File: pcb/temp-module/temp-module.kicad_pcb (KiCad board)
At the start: 2 copper layers, 37 x 27 mm, 14 parts, among them J1 Connector_male, J2 Screw_Terminal_01x02, U1 MCP6002-xSN

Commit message: update pcb
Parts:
- J2: footprint TerminalBlock:TerminalBlock_bornier-2_P5.08mm -> TerminalBlock_Phoenix:TerminalBlock_Phoenix_MKDS-1,5-2-5.08_1x02_P5.08mm_Horizontal
- R1: value 1.3K -> 110K
- R3: value 5.1K -> 1.3K
- R4: value 330R -> 5.1K
- R5: value 5.1K -> 330R
- R6: value 110K -> 5.1K
- moved R3 17.2 mm to (150.9, 101.0)
- moved R6 17.1 mm to (166.5, 101.0)
- moved R1 7.09 mm to (150.9, 94.0)
- moved J2 5.21 mm to (157.4, 111.0), turned to 0 degrees
- moved R4 3.90 mm to (166.5, 94.0)
- moved R5 3.89 mm to (166.5, 97.5)
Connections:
- R1 pad 1: S1 -> /U5_OP-
- R1 pad 2: GND -> SREG
- R3 pad 1: GND -> S1
- R3 pad 2: /R4-5 -> GND
- R4 pad 1: /R4-5 -> +5V
- R5 pad 1: +5V -> /R4-5
- R6 pad 1: /U5_OP- -> GND
- R6 pad 2: SREG -> /R4-5
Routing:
- net SREG: track 65.3 -> 30.1 mm
- net +5V: track 78.5 -> 63.4 mm
- net S1: track 21.4 -> 16.6 mm
- net GND: track 33.6 -> 32.4 mm
- net /U5_OP+: track 22.0 -> 20.8 mm
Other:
- board text added: "Sensor"

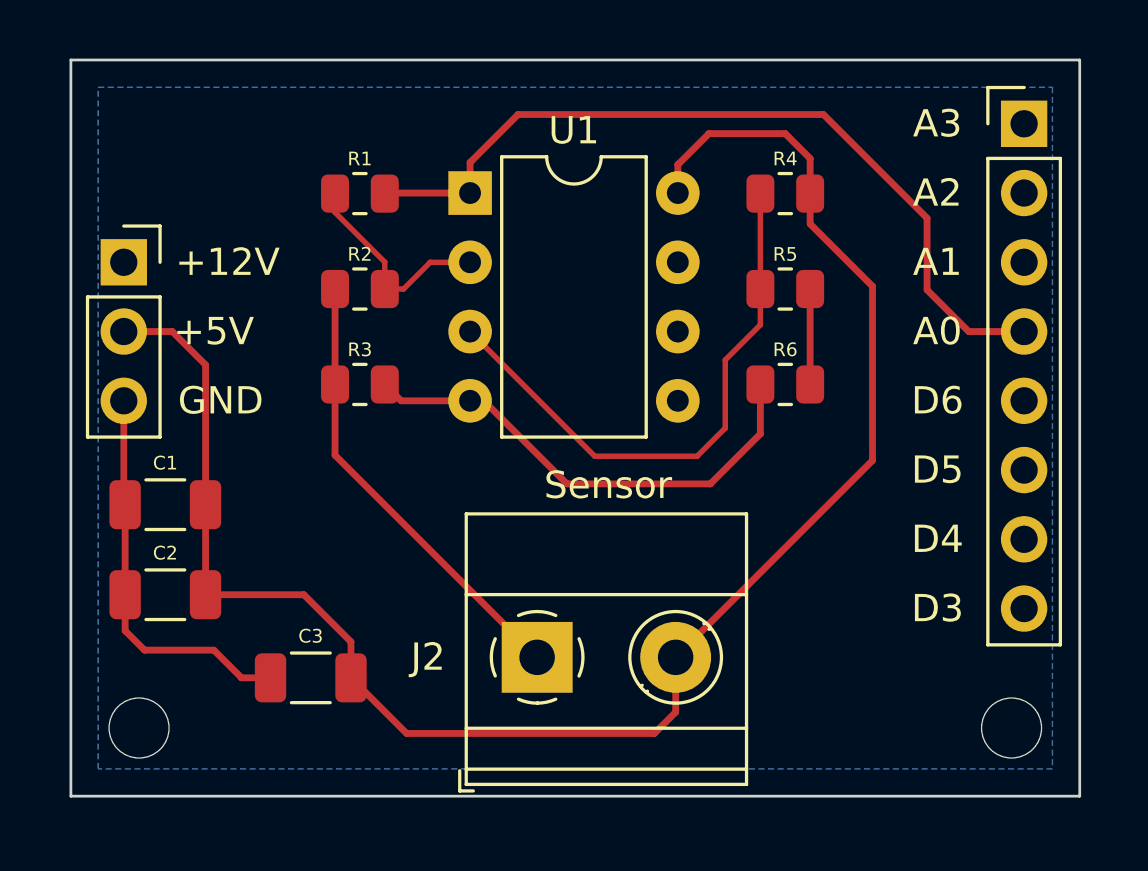
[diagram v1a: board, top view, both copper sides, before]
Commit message: added AVRISP adapter to pcb
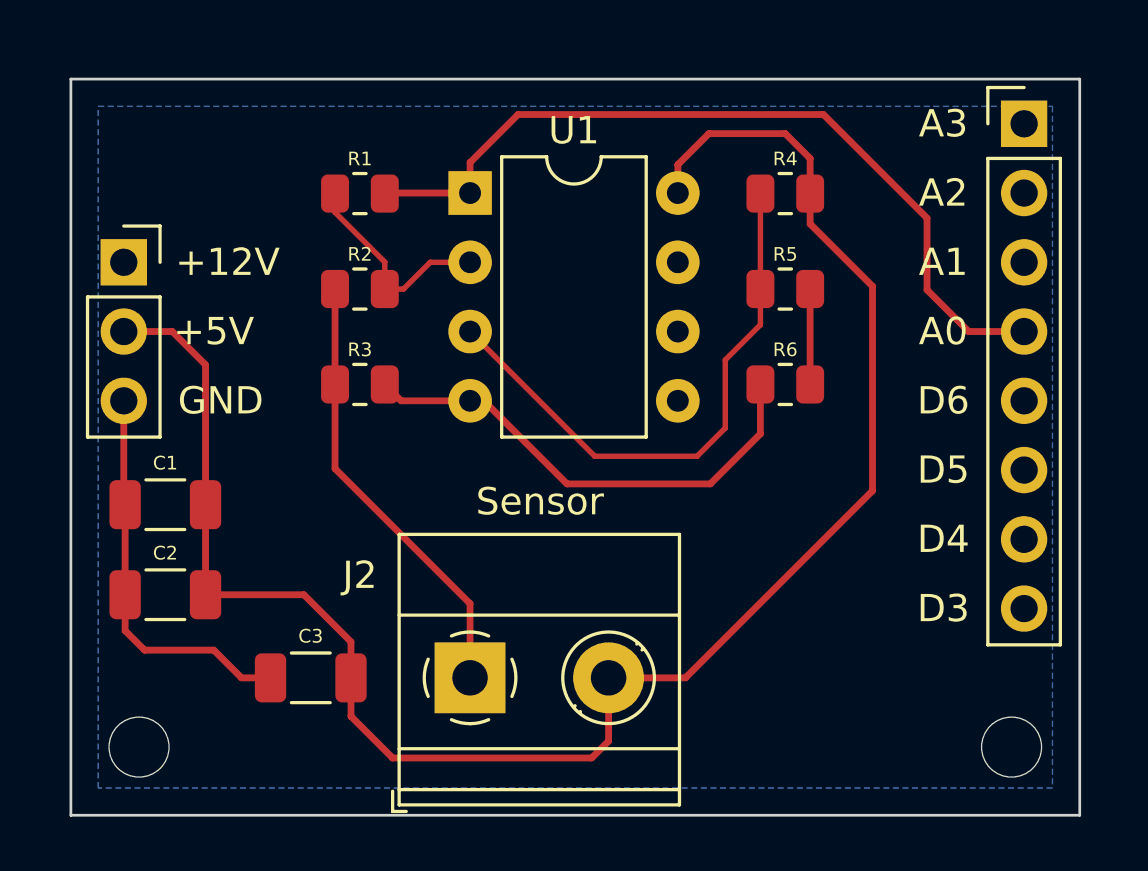
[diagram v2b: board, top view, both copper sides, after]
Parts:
- moved J2 2.57 mm to (154.9, 111.8)
- moved REF** 0.70 mm to (174.8, 114.3)
- moved REF** 0.70 mm to (142.8, 114.3)
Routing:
- net +5V: track 63.4 -> 65.8 mm
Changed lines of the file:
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@@
       (effects (font (size 1 1) (thickness 0.15)))
     )
-    (fp_text user "D4" (at 14.605 7.62 unlocked) (layer "F.SilkS")
-      (effects (font (size 1 1) (thickness 0.15)))
-    )
-    (fp_text user "A1" (at 14.605 -2.54 unlocked) (layer "F.SilkS")
-      (effects (font (size 1 1) (thickness 0.15)))
-    )
-    (fp_text user "A0" (at 14.605 0 unlocked) (layer "F.SilkS")
-      (effects (font (size 1 1) (thickness 0.15)))
-    )
-    (fp_text user "D3" (at 14.605 10.16 unlocked) (layer "F.SilkS")
-      (effects (font (size 1 1) (thickness 0.15)))
-    )
-    (fp_text user "D5" (at 14.605 5.08 unlocked) (layer "F.SilkS")
+    (fp_text user "D4" (at 14.82 7.62 unlocked) (layer "F.SilkS")
+      (effects (font (size 1 1) (thickness 0.15)))
+    )
+    (fp_text user "A1" (at 14.82 -2.54 unlocked) (layer "F.SilkS")
+      (effects (font (size 1 1) (thickness 0.15)))
+    )
+    (fp_text user "A0" (at 14.82 0 unlocked) (layer "F.SilkS")
+      (effects (font (size 1 1) (thickness 0.15)))
+    )
+    (fp_text user "D3" (at 14.82 10.16 unlocked) (layer "F.SilkS")
+      (effects (font (size 1 1) (thickness 0.15)))
+    )
+    (fp_text user "D5" (at 14.82 5.08 unlocked) (layer "F.SilkS")
       (effects (font (size 1 1) (thickness 0.15)))
     )
@@
       (effects (font (size 1 1) (thickness 0.15)))
     )
-    (fp_text user "A3" (at 14.605 -7.62 unlocked) (layer "F.SilkS")
-      (effects (font (size 1 1) (thickness 0.15)))
-    )
-    (fp_text user "A2" (at 14.605 -5.08 unlocked) (layer "F.SilkS")
-      (effects (font (size 1 1) (thickness 0.15)))
-    )
-    (fp_text user "D6" (at 14.605 2.54 unlocked) (layer "F.SilkS")
+    (fp_text user "A3" (at 14.82 -7.62 unlocked) (layer "F.SilkS")
+      (effects (font (size 1 1) (thickness 0.15)))
+    )
+    (fp_text user "A2" (at 14.82 -5.08 unlocked) (layer "F.SilkS")
+      (effects (font (size 1 1) (thickness 0.15)))
+    )
+    (fp_text user "D6" (at 14.82 2.54 unlocked) (layer "F.SilkS")
       (effects (font (size 1 1) (thickness 0.15)))
     )
@@
   )
   (footprint "MountingHole:MountingHole_2.2mm_M2" (layer "F.Cu")
-    (at 174.8 113.6)
+    (at 174.8 114.3)
     (descr "Mounting Hole 2.2mm, no annular, M2")
     (tags "mounting hole 2.2mm no annular m2")
@@
   )
   (footprint "MountingHole:MountingHole_2.2mm_M2" (layer "F.Cu")
-    (at 142.8 113.6)
+    (at 142.8 114.3)
     (descr "Mounting Hole 2.2mm, no annular, M2")
     (tags "mounting hole 2.2mm no annular m2")
@@
   )
   (footprint "TerminalBlock_Phoenix:TerminalBlock_Phoenix_MKDS-1,5-2-5.08_1x02_P5.08mm_Horizontal" (layer "F.Cu")
-    (at 157.4 111.0085)
+    (at 154.94 111.76)
     (descr "Terminal Block Phoenix MKDS-1,5-2-5.08, 2 pins, pitch 5.08mm, size 10.2x9.8mm^2, drill diamater 1.3mm, pad diameter 2.6mm, see http://www.farnell.com/datasheets/100425.pdf, script-generated using https://github.com/pointhi/kicad-footprint-generator/scripts/TerminalBlock_Phoenix")
     (tags "THT Terminal Block Phoenix MKDS-1,5-2-5.08 pitch 5.08mm size 10.2x9.8mm^2 drill 1.3mm pad 2.6mm")
@@
     (property "Sheetname" "")
     (attr through_hole)
-    (fp_text reference "J2" (at -4 -0.0085) (layer "F.SilkS")
+    (fp_text reference "J2" (at -4.04 -3.76) (layer "F.SilkS")
       (effects (font (size 1 1) (thickness 0.15)))
     )
@@
     )
   )
-  (gr_line (start 140.3 89.1) (end 140.3 116.1) (layer "Edge.Cuts") (width 0.1))
-  (gr_line (start 177.3 89.1) (end 140.3 89.1) (layer "Edge.Cuts") (width 0.1))
-  (gr_line (start 140.3 116.1) (end 177.3 116.1) (layer "Edge.Cuts") (width 0.1))
-  (gr_line (start 177.3 116.1) (end 177.3 89.1) (layer "Edge.Cuts") (width 0.1))
+  (gr_line (start 140.3 89.8) (end 140.3 116.8) (layer "Edge.Cuts") (width 0.1))
+  (gr_line (start 177.3 89.8) (end 140.3 89.8) (layer "Edge.Cuts") (width 0.1))
+  (gr_line (start 140.3 116.8) (end 177.3 116.8) (layer "Edge.Cuts") (width 0.1))
+  (gr_line (start 177.3 116.8) (end 177.3 89.8) (layer "Edge.Cuts") (width 0.1))
   (gr_text "GND" (at 145.796 101.6) (layer "F.SilkS")
     (effects (font (size 1 1) (thickness 0.15)))
   )
-  (gr_text "Sensor" (at 160 104.7) (layer "F.SilkS")
+  (gr_text "Sensor" (at 157.5 105.3) (layer "F.SilkS")
     (effects (font (size 1 1) (thickness 0.15)))
   )
-  (segment (start 149.9875 103.596) (end 157.4 111.0085) (width 0.25) (layer "F.Cu") (net 1))
-  (segment (start 149.9875 101) (end 149.9875 103.596) (width 0.25) (layer "F.Cu") (net 1))
+  (segment (start 154.94 109.04) (end 149.9875 104.0875) (width 0.25) (layer "F.Cu") (net 1))
   (segment (start 149.9875 97.5) (end 149.9875 101) (width 0.25) (layer "F.Cu") (net 1))
-  (segment (start 162.48 113.02) (end 162.48 111.0085) (width 0.25) (layer "F.Cu") (net 2))
-  (segment (start 152.613 113.8) (end 161.7 113.8) (width 0.25) (layer "F.Cu") (net 2))
+  (segment (start 149.9875 104.0875) (end 149.9875 101) (width 0.25) (layer "F.Cu") (net 1))
+  (segment (start 154.94 111.76) (end 154.94 109.04) (width 0.25) (layer "F.Cu") (net 1))
+  (segment (start 152.1 114.7) (end 159.4 114.7) (width 0.25) (layer "F.Cu") (net 2))
   (segment (start 145.239 100.281) (end 144.018 99.06) (width 0.25) (layer "F.Cu") (net 2))
   (segment (start 144.018 99.06) (end 142.24 99.06) (width 0.25) (layer "F.Cu") (net 2))
+  (segment (start 150.573 111.76) (end 150.573 113.173) (width 0.25) (layer "F.Cu") (net 2))
   (segment (start 150.573 111.76) (end 150.573 110.441) (width 0.25) (layer "F.Cu") (net 2))
+  (segment (start 159.4 114.7) (end 160.02 114.08) (width 0.25) (layer "F.Cu") (net 2))
   (segment (start 163.7 91.8) (end 162.56 92.94) (width 0.25) (layer "F.Cu") (net 2))
   (segment (start 167.4125 92.7125) (end 166.5 91.8) (width 0.25) (layer "F.Cu") (net 2))
+  (segment (start 169.7 104.9) (end 169.7 97.4) (width 0.25) (layer "F.Cu") (net 2))
   (segment (start 167.4125 94) (end 167.4125 92.7125) (width 0.25) (layer "F.Cu") (net 2))
+  (segment (start 160.02 111.76) (end 162.84 111.76) (width 0.25) (layer "F.Cu") (net 2))
   (segment (start 148.844 108.712) (end 150.573 110.441) (width 0.25) (layer "F.Cu") (net 2))
-  (segment (start 169.7 103.7885) (end 169.7 97.4) (width 0.25) (layer "F.Cu") (net 2))
   (segment (start 145.239 105.41) (end 145.239 108.712) (width 0.25) (layer "F.Cu") (net 2))
   (segment (start 166.5 91.8) (end 163.7 91.8) (width 0.25) (layer "F.Cu") (net 2))
-  (segment (start 150.573 111.76) (end 152.613 113.8) (width 0.25) (layer "F.Cu") (net 2))
+  (segment (start 162.84 111.76) (end 169.7 104.9) (width 0.25) (layer "F.Cu") (net 2))
+  (segment (start 169.7 97.4) (end 167.4125 95.1125) (width 0.25) (layer "F.Cu") (net 2))
   (segment (start 167.4125 95.1125) (end 167.4125 94) (width 0.25) (layer "F.Cu") (net 2))
-  (segment (start 169.7 97.4) (end 167.4125 95.1125) (width 0.25) (layer "F.Cu") (net 2))
+  (segment (start 160.02 114.08) (end 160.02 111.76) (width 0.25) (layer "F.Cu") (net 2))
   (segment (start 145.239 108.712) (end 148.844 108.712) (width 0.25) (layer "F.Cu") (net 2))
-  (segment (start 162.48 111.0085) (end 169.7 103.7885) (width 0.25) (layer "F.Cu") (net 2))
   (segment (start 145.239 100.281) (end 145.239 105.41) (width 0.25) (layer "F.Cu") (net 2))
-  (segment (start 161.7 113.8) (end 162.48 113.02) (width 0.25) (layer "F.Cu") (net 2))
+  (segment (start 150.573 113.173) (end 152.1 114.7) (width 0.25) (layer "F.Cu") (net 2))
   (segment (start 162.56 92.94) (end 162.56 93.98) (width 0.25) (layer "F.Cu") (net 2))
   (segment (start 158.496 104.648) (end 155.448 101.6) (width 0.25) (layer "F.Cu") (net 3))
@@
     (polygon
       (pts
-        (xy 176.3 115.1)
-        (xy 141.3 115.1)
-        (xy 141.3 90.1)
-        (xy 176.3 90.1)
+        (xy 176.3 115.8)
+        (xy 141.3 115.8)
+        (xy 141.3 90.8)
+        (xy 176.3 90.8)
       )
     )

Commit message: m12 plug; j1939 transition
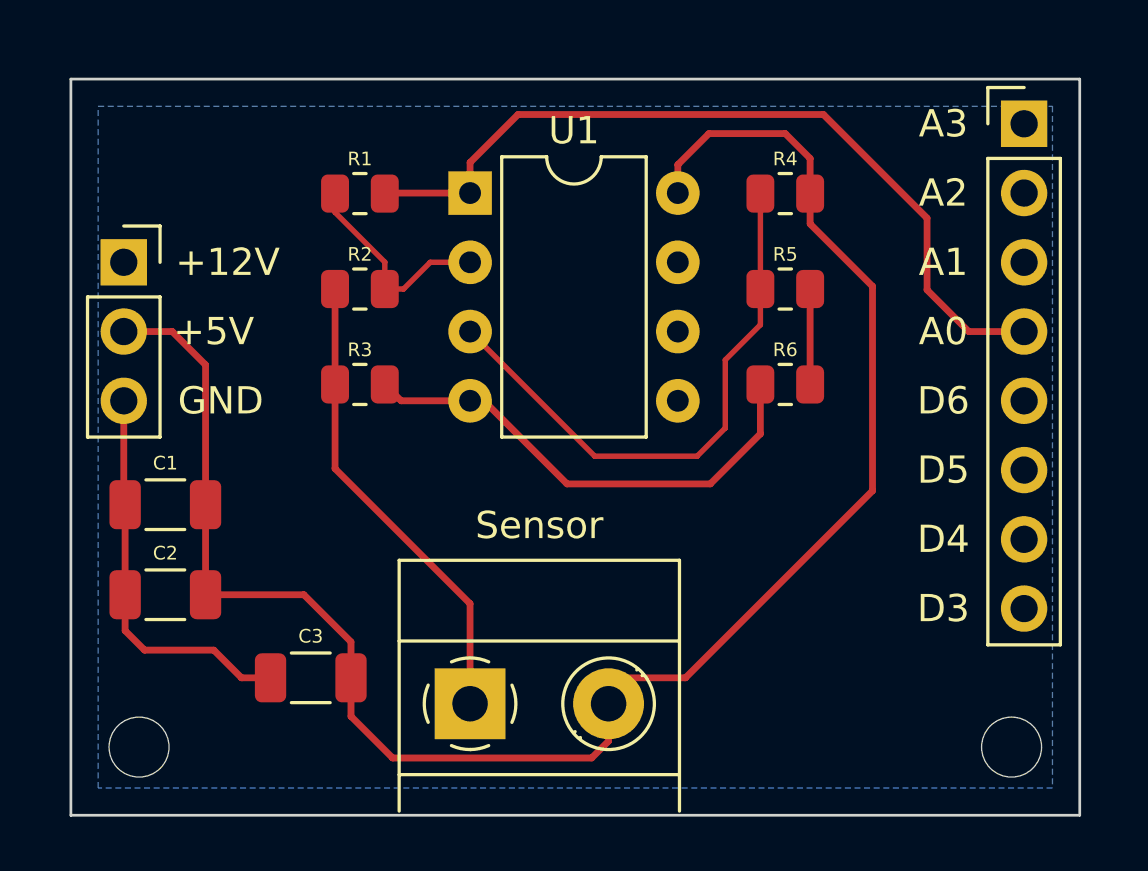
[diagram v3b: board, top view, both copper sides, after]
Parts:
- moved J2 0.95 mm to (154.9, 112.7)
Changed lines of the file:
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@@
   )
   (footprint "TerminalBlock_Phoenix:TerminalBlock_Phoenix_MKDS-1,5-2-5.08_1x02_P5.08mm_Horizontal" (layer "F.Cu")
-    (at 154.94 111.76)
+    (at 154.94 112.71)
     (descr "Terminal Block Phoenix MKDS-1,5-2-5.08, 2 pins, pitch 5.08mm, size 10.2x9.8mm^2, drill diamater 1.3mm, pad diameter 2.6mm, see http://www.farnell.com/datasheets/100425.pdf, script-generated using https://github.com/pointhi/kicad-footprint-generator/scripts/TerminalBlock_Phoenix")
     (tags "THT Terminal Block Phoenix MKDS-1,5-2-5.08 pitch 5.08mm size 10.2x9.8mm^2 drill 1.3mm pad 2.6mm")
@@
     (property "Sheetname" "")
     (attr through_hole)
-    (fp_text reference "J2" (at -4.04 -3.76) (layer "F.SilkS")
+    (fp_text reference "J2" (at -4.04 -3.76) (layer "F.SilkS") hide
       (effects (font (size 1 1) (thickness 0.15)))
     )
@@
       (effects (font (size 1 1) (thickness 0.15)))
     )
-    (fp_text user "${REFERENCE}" (at 2.54 3.2) (layer "F.Fab")
+    (fp_text user "${REFERENCE}" (at 2.54 -3.744) (layer "F.Fab")
       (effects (font (size 1 1) (thickness 0.15)))
     )
     (fp_line (start 6.355 -1.069) (end 6.308 -1.023) (layer "F.SilkS") (width 0.12))
-    (fp_line (start -2.84 4.16) (end -2.84 4.9) (layer "F.SilkS") (width 0.12))
     (fp_line (start 6.15 -1.275) (end 6.115 -1.239) (layer "F.SilkS") (width 0.12))
-    (fp_line (start -2.6 4.1) (end 7.68 4.1) (layer "F.SilkS") (width 0.12))
     (fp_line (start -2.6 -2.301) (end 7.68 -2.301) (layer "F.SilkS") (width 0.12))
     (fp_line (start 3.853 1.023) (end 3.806 1.069) (layer "F.SilkS") (width 0.12))
     (fp_line (start 4.046 1.239) (end 4.011 1.274) (layer "F.SilkS") (width 0.12))
-    (fp_line (start -2.6 4.66) (end 7.68 4.66) (layer "F.SilkS") (width 0.12))
-    (fp_line (start -2.84 4.9) (end -2.34 4.9) (layer "F.SilkS") (width 0.12))
     (fp_line (start -2.6 2.6) (end 7.68 2.6) (layer "F.SilkS") (width 0.12))
-    (fp_line (start 7.68 -5.261) (end 7.68 4.66) (layer "F.SilkS") (width 0.12))
-    (fp_line (start -2.6 -5.261) (end -2.6 4.66) (layer "F.SilkS") (width 0.12))
+    (fp_line (start 7.68 -5.261) (end 7.68 3.937) (layer "F.SilkS") (width 0.12))
+    (fp_line (start -2.6 -5.261) (end -2.6 3.937) (layer "F.SilkS") (width 0.12))
     (fp_line (start -2.6 -5.261) (end 7.68 -5.261) (layer "F.SilkS") (width 0.12))
     (fp_arc (start 0.683318 1.534756) (mid 0.349292 1.643288) (end 0 1.68) (layer "F.SilkS") (width 0.12))
@@
     (fp_arc (start 0.028805 1.680253) (mid -0.335551 1.646659) (end -0.684 1.535) (layer "F.SilkS") (width 0.12))
     (fp_circle (center 5.08 0) (end 6.76 0) (layer "F.SilkS") (width 0.12) (fill none))
-    (fp_line (start 8.13 5.1) (end 8.13 -5.71) (layer "F.CrtYd") (width 0.05))
+    (fp_line (start 8.128 4.064) (end 8.13 -5.71) (layer "F.CrtYd") (width 0.05))
     (fp_line (start 8.13 -5.71) (end -3.04 -5.71) (layer "F.CrtYd") (width 0.05))
-    (fp_line (start -3.04 5.1) (end 8.13 5.1) (layer "F.CrtYd") (width 0.05))
-    (fp_line (start -3.04 -5.71) (end -3.04 5.1) (layer "F.CrtYd") (width 0.05))
+    (fp_line (start -3.048 4.064) (end 8.128 4.064) (layer "F.CrtYd") (width 0.05))
+    (fp_line (start -3.04 -5.71) (end -3.048 4.064) (layer "F.CrtYd") (width 0.05))
     (fp_line (start 6.218 -0.955) (end 4.126 1.138) (layer "F.Fab") (width 0.1))
-    (fp_line (start -2.04 4.6) (end -2.54 4.1) (layer "F.Fab") (width 0.1))
     (fp_line (start -2.54 -2.3) (end 7.62 -2.3) (layer "F.Fab") (width 0.1))
     (fp_line (start -2.54 2.6) (end 7.62 2.6) (layer "F.Fab") (width 0.1))
-    (fp_line (start 7.62 -5.2) (end 7.62 4.6) (layer "F.Fab") (width 0.1))
+    (fp_line (start 7.62 -5.2) (end 7.62 3.81) (layer "F.Fab") (width 0.1))
     (fp_line (start 1.138 -0.955) (end -0.955 1.138) (layer "F.Fab") (width 0.1))
     (fp_line (start -2.54 -5.2) (end 7.62 -5.2) (layer "F.Fab") (width 0.1))
     (fp_line (start 6.035 -1.138) (end 3.943 0.955) (layer "F.Fab") (width 0.1))
-    (fp_line (start -2.54 4.1) (end 7.62 4.1) (layer "F.Fab") (width 0.1))
     (fp_line (start 0.955 -1.138) (end -1.138 0.955) (layer "F.Fab") (width 0.1))
-    (fp_line (start -2.54 4.1) (end -2.54 -5.2) (layer "F.Fab") (width 0.1))
-    (fp_line (start 7.62 4.6) (end -2.04 4.6) (layer "F.Fab") (width 0.1))
+    (fp_line (start -2.54 3.81) (end -2.54 -5.2) (layer "F.Fab") (width 0.1))
     (fp_circle (center 5.08 0) (end 6.58 0) (layer "F.Fab") (width 0.1) (fill none))
     (fp_circle (center 0 0) (end 1.5 0) (layer "F.Fab") (width 0.1) (fill none))
@@
     (effects (font (size 1 1) (thickness 0.15)))
   )
-  (gr_text "Sensor" (at 157.5 105.3) (layer "F.SilkS")
+  (gr_text "Sensor" (at 157.48 106.172) (layer "F.SilkS")
     (effects (font (size 1 1) (thickness 0.15)))
   )

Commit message: temp-calibrate
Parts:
- removed R1: 110K, Resistor_SMD:R_0805_2012Metric
- removed R2: 10K, Resistor_SMD:R_0805_2012Metric
- removed R4, R6: 5.1K, Resistor_SMD:R_0805_2012Metric
- added C4: 100nF, Capacitor_SMD:C_1206_3216Metric, B.Cu at (169.7, 99.1)
- added R1_1: 1.3k, Resistor_SMD:R_0805_2012Metric, F.Cu at (151.9, 94.5)
- added R1_2: 2k, Resistor_SMD:R_0805_2012Metric, F.Cu at (149.1, 95.5)
- added R1_3: 10k, Resistor_SMD:R_0805_2012Metric, F.Cu at (151.9, 96.5)
- added R2_1: 330, Resistor_SMD:R_0805_2012Metric, F.Cu at (165.6, 98.8)
- added R2_2: 1.3k, Resistor_SMD:R_0805_2012Metric, F.Cu at (168.4, 97.8)
- added R2_3: 110k, Resistor_SMD:R_0805_2012Metric, F.Cu at (165.6, 96.8)
- added R4_1: 2k, Resistor_SMD:R_0805_2012Metric, F.Cu at (145.9, 107.8)
- added R4_2: 2.4k, Resistor_SMD:R_0805_2012Metric, F.Cu at (146.9, 110.6)
- added R4_3: 20k, Resistor_SMD:R_0805_2012Metric, F.Cu at (147.9, 107.8)
- C1, C2: value 0.1uF -> 100nF; moved to B.Cu
- C3: moved to B.Cu
- J2: value Screw_Terminal_01x02 -> Screw_Terminal_01x03; footprint TerminalBlock_Phoenix:TerminalBlock_Phoenix_MKDS-1,5-2-5.08_1x02_P5.08mm_Horizontal -> Connector_Wago:Wago_734-163_1x03_P3.50mm_Horizontal
- R3: value 1.3K -> 20k
- R5: value 330R -> 1k
- U1: value MCP6002-xSN -> MCP6002-xP
- moved R3 21.0 mm to (169.8, 91.8), turned to 180 degrees
- moved R5 12.1 mm to (169.4, 109.2), turned to 90 degrees
- moved C2 7.82 mm to (148.3, 102.4), turned to 180 degrees
- moved C1 7.82 mm to (148.3, 99.1), turned to 0 degrees
- moved C3 6.40 mm to (148.3, 105.4), turned to 0 degrees
- moved J2 4.47 mm to (155.2, 108.2)
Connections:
- J2 pad 2: +5V -> /S2
- R3 pad 1: S1 -> +5V
- R3 pad 2: GND -> /vk_in
- R5 pad 1: /R4-5 -> /S2
- R5 pad 2: /U5_OP+ -> +5V
- U1 pad 1: SREG -> /vk_buf
- U1 pad 2: /U5_OP- -> /vk_buf
- U1 pad 3: /U5_OP+ -> /vk_in
- U1 pad 5: (no net) -> S1
- U1 pad 6: (no net) -> /fb
- U1 pad 7: (no net) -> SREG
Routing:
- net /vk_in: track 0.00 -> 42.8 mm
- net /U5_OP+: track 20.8 -> 0.00 mm
- net /S2: track 0.00 -> 18.7 mm
- net GND: track 32.4 -> 16.4 mm, vias 0 -> 4
- net /fb: track 0.00 -> 13.3 mm
- net SREG: track 30.1 -> 17.1 mm, vias 0 -> 1
- net /U5_OP-: track 7.79 -> 0.00 mm
- net /vk_buf: track 0.00 -> 4.89 mm
- net S1: track 16.3 -> 11.9 mm
- net /R4-5: track 3.50 -> 0.00 mm
- net /R_4_2_3: track 0.00 -> 2.07 mm
- net /R_4_1_2: track 0.00 -> 2.07 mm
- net /R_2_2_3: track 0.00 -> 1.92 mm
- net /R_2_1_2: track 0.00 -> 1.92 mm
- net /R_1_2_3: track 0.00 -> 1.92 mm
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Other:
- board text added: "R1"
- board text added: "R2"
- board text added: "R4"
